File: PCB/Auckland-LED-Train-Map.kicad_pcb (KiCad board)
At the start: 2 copper layers, 249 x 66 mm, 260 parts, among them J1 Conn_01x06_Socket, Q1 HL3415A, Q2 MMBT3904, U1 XC6206P332MR, U2 ESP32-C3FH4, U3 SN74LVC4245APWR, U4 Connector, USB-TYPE-C-16P, U5 Connector, USB-TYPE-C-16P, X1 40MHz, 15pF

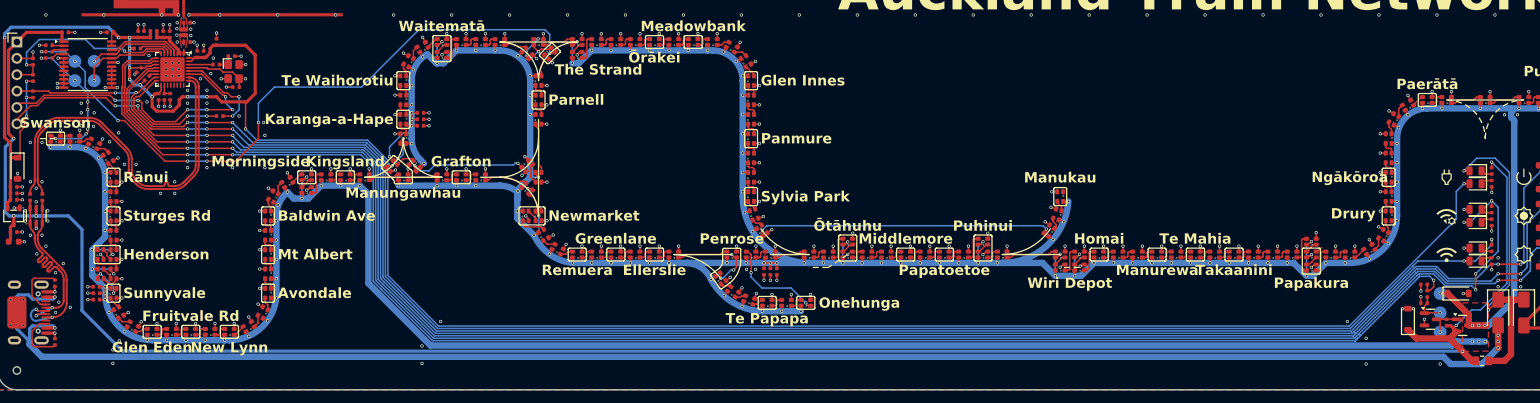
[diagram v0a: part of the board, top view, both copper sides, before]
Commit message: - Add Readme - V1 RC3 PCB - Tidy up Schematic - Add Datasheets
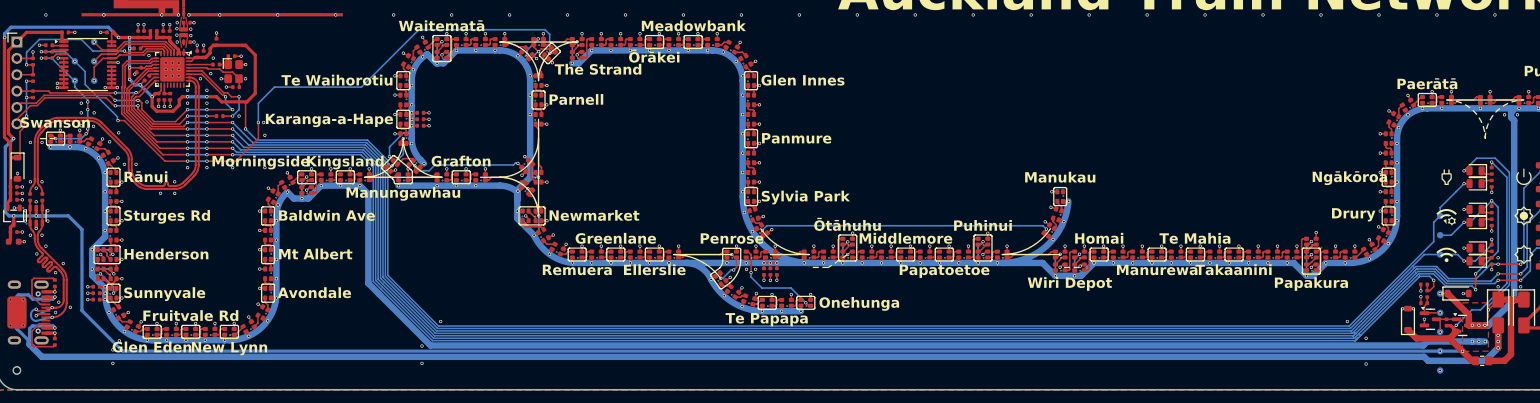
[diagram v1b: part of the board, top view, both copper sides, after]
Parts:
- removed TP1: NAL-NIMT_LED, Custom_Footprints:TestPoint_Pad_D2.0mm
- removed TP4: STRAND-MNK_LED, Custom_Footprints:TestPoint_Pad_D2.0mm
- added TP10: VBUS, Custom_Footprints:TestPoint_Pad_D1.0mm, B.Cu at (224.0, 60.0)
- added TP11: GND, Custom_Footprints:TestPoint_Pad_D1.0mm, B.Cu at (224.0, 63.0)
- added TP12: WiFi_LED, Custom_Footprints:TestPoint_Pad_D1.0mm, B.Cu at (224.0, 45.0)
- added TP13: 3.3V, Custom_Footprints:TestPoint_Pad_D1.0mm, B.Cu at (224.0, 39.0)
- added TP14: Config_LED, Custom_Footprints:TestPoint_Pad_D1.0mm, B.Cu at (224.0, 42.0)
- added TP15: LVL-Shifter-EN, Custom_Footprints:TestPoint_Pad_D1.0mm, B.Cu at (15.0, 12.0)
- added TP3: NAL-NIMT_LED, Custom_Footprints:TestPoint_Pad_D1.0mm, B.Cu at (12.0, 18.0)
- added TP9: STRAND-MNK_LED, Custom_Footprints:TestPoint_Pad_D1.0mm, B.Cu at (12.0, 15.0)
- J1: value Conn_01x06_Socket -> Prog Connector; footprint Connector_PinHeader_2.54mm:PinHeader_1x06_P2.54mm_Vertical -> Custom_Footprints:Prog Connector
- TP2, TP5, TP7, TP8: footprint Custom_Footprints:TestPoint_Pad_D2.0mm -> Custom_Footprints:TestPoint_Pad_D1.0mm
- TP6: value LED_+5V -> ALED_5V; footprint Custom_Footprints:TestPoint_Pad_D2.0mm -> Custom_Footprints:TestPoint_Pad_D1.0mm
- turned TP2 to 0 degrees
- turned TP8 to 0 degrees
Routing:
- net /CONFIG_LED: track 275.5 -> 280.0 mm
- net /LVL_Shifter_EN_Active_Low: track 11.3 -> 14.5 mm, vias 0 -> 1
- net /WIFI_LED: track 250.0 -> 250.8 mm
- net VBUS: vias 6 -> 7

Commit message: Fix charlieplexed LEDs D10 and D11
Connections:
- D10 pad 2: GND -> +3V3
- D11 pad 2: GND -> +3V3
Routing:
- net +3V3: track 360.9 -> 370.6 mm, vias 15 -> 17
- net GND: track 208.2 -> 206.5 mm, vias 320 -> 318
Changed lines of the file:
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@@
 			(layers "F.Cu" "F.Mask" "F.Paste")
 			(roundrect_rratio 0.25)
-			(net 1 "GND")
+			(net 2 "+3V3")
 			(pintype "passive")
 		)
@@
 			(layers "F.Cu" "F.Mask" "F.Paste")
 			(roundrect_rratio 0.25)
-			(net 1 "GND")
+			(net 2 "+3V3")
 			(pintype "passive")
 		)
@@
 	)
 	(segment
-		(start 228.560001 44)
-		(end 227.710002 44)
-		(width 0.25)
-		(layer "F.Cu")
-		(net 1)
-	)
-	(segment
 		(start 48.75 34.55)
 		(end 48.45 34.55)
@@
 	)
 	(segment
-		(start 228.560001 38)
-		(end 227.710002 38)
-		(width 0.25)
-		(layer "F.Cu")
-		(net 1)
-	)
-	(segment
 		(start 126.749999 44.55)
 		(end 126.749999 43.7)
@@
 	)
 	(via
-		(at 227.710002 38)
-		(size 0.5)
-		(drill 0.3)
-		(layers "F.Cu" "B.Cu")
-		(net 1)
-	)
-	(via
 		(at 19.3 48.75)
 		(size 0.5)
@@
 	)
 	(via
-		(at 227.710002 44)
-		(size 0.5)
-		(drill 0.3)
-		(layers "F.Cu" "B.Cu")
-		(net 1)
-	)
-	(via
 		(at 212.999518 42.69532)
 		(size 0.5)
@@
 	)
 	(segment
+		(start 228.560001 44)
+		(end 227.710002 44)
+		(width 0.25)
+		(layer "F.Cu")
+		(net 2)
+	)
+	(segment
 		(start 28.2 21)
 		(end 28.2 21.8)
@@
 	)
 	(segment
+		(start 228.560001 38)
+		(end 227.710002 38)
+		(width 0.25)
+		(layer "F.Cu")
+		(net 2)
+	)
+	(segment
 		(start 34 20.5)
 		(end 32.5 20.5)
@@
 	)
 	(via
+		(at 227.710002 38)
+		(size 0.5)
+		(drill 0.3)
+		(layers "F.Cu" "B.Cu")
+		(net 2)
+	)
+	(via
 		(at 4.5 20.62)
 		(size 0.5)
@@
 	)
 	(via
+		(at 227.710002 44)
+		(size 0.5)
+		(drill 0.3)
+		(layers "F.Cu" "B.Cu")
+		(net 2)
+	)
+	(via
 		(at 20.5 16)
 		(size 0.5)
@@
 	)
 	(segment
+		(start 224 44)
+		(end 223 43)
+		(width 0.25)
+		(layer "B.Cu")
+		(net 2)
+	)
+	(segment
 		(start 223 40)
 		(end 223 43)
@@
 	)
 	(segment
+		(start 225.705001 36.005001)
+		(end 226.5 35.210002)
+		(width 0.25)
+		(layer "B.Cu")
+		(net 2)
+	)
+	(segment
 		(start 224 39)
 		(end 224 37.710002)
@@
 	)
 	(segment
+		(start 227.7 38)
+		(end 225.705001 36.005001)
+		(width 0.25)
+		(layer "B.Cu")
+		(net 2)
+	)
+	(segment
 		(start 224 37.710002)
-		(end 226.5 35.210002)
+		(end 225.705001 36.005001)
 		(width 0.25)
 		(layer "B.Cu")
@@
 	)
 	(segment
+		(start 227.710002 44)
+		(end 224 44)
+		(width 0.25)
+		(layer "B.Cu")
+		(net 2)
+	)
+	(segment
 		(start 40.232 27.232)
 		(end 57.435646 27.232)
@@
 		(width 0.25)
 		(layer "B.Cu")
+		(net 2)
+	)
+	(segment
+		(start 227.710002 38)
+		(end 227.7 38)
+		(width 0.25)
+		(layer "B.Cu")

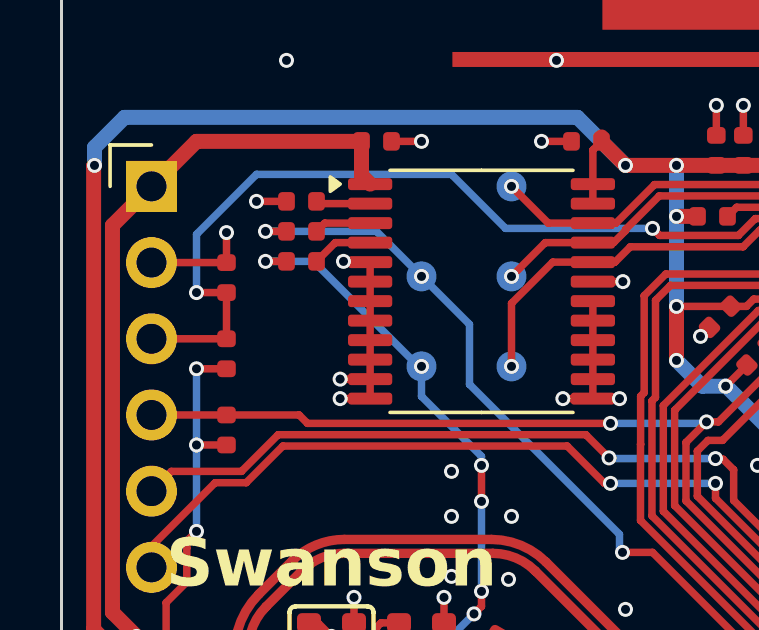
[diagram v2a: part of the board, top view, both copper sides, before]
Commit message: Add changes suggested from reddit
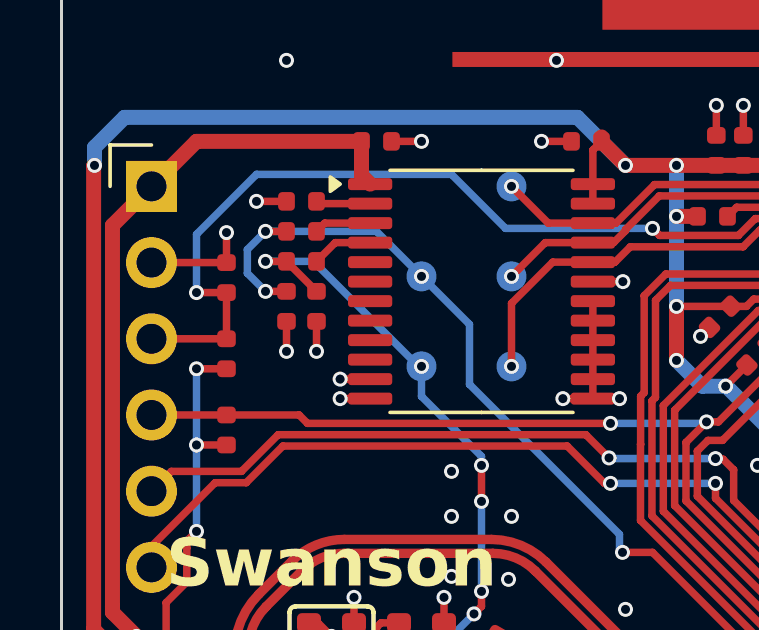
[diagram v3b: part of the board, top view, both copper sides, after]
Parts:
- added R24: 100kΩ, PCM_JLCPCB:R_0402, F.Cu at (8.50, 16.0)
- added R25: 100kΩ, PCM_JLCPCB:R_0402, F.Cu at (7.50, 16.0)
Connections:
- U3 pad 10: GND -> unconnected-(U3-A8-Pad10)
- U3 pad 5: GND -> unconnected-(U3-A3-Pad5)
- U3 pad 6: GND -> unconnected-(U3-A4-Pad6)
- U3 pad 7: GND -> unconnected-(U3-A5-Pad7)
- U3 pad 8: GND -> unconnected-(U3-A6-Pad8)
- U3 pad 9: GND -> unconnected-(U3-A7-Pad9)
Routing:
- net GND: track 206.5 -> 203.1 mm, vias 318 -> 319
- net STRAND-MNK-1: track 104.0 -> 107.2 mm, vias 8 -> 9
- net NAL-NIMT-1: track 22.5 -> 23.9 mm
